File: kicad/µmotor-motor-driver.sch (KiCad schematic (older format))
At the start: 12 parts, among them Q301 FDMD82xx, Q302 FDMD82xx, Q303 FDMD82xx, U301 DRV8323S

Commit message: layout: improvements and silkscreen
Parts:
- R301, R302, R303: footprint Resistors_SMD:R_0603 -> Resistors_SMD:R_0805
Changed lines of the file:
@@
 $EndDescr
 $Comp
-L +24V #PWR015
+L +24V #PWR017
 U 1 1 59BA7201
 P 2100 2800
-F 0 "#PWR015" H 2100 2650 50  0001 C CNN
+F 0 "#PWR017" H 2100 2650 50  0001 C CNN
 F 1 "+24V" H 2100 2940 50  0000 C CNN
 F 2 "" H 2100 2800 50  0001 C CNN
@@
 $EndComp
 $Comp
-L GND #PWR016
+L GND #PWR018
 U 1 1 5A4FE4D1
 P 2300 3400
-F 0 "#PWR016" H 2300 3150 50  0001 C CNN
+F 0 "#PWR018" H 2300 3150 50  0001 C CNN
 F 1 "GND" H 2300 3250 50  0000 C CNN
 F 2 "" H 2300 3400 50  0001 C CNN
@@
 $EndComp
 $Comp
-L GND #PWR017
+L GND #PWR019
 U 1 1 5A4FE4F8
 P 2950 3400
-F 0 "#PWR017" H 2950 3150 50  0001 C CNN
+F 0 "#PWR019" H 2950 3150 50  0001 C CNN
 F 1 "GND" H 2950 3250 50  0000 C CNN
 F 2 "" H 2950 3400 50  0001 C CNN
@@
 $EndComp
 $Comp
-L GND #PWR018
+L GND #PWR020
 U 1 1 5A4FE87C
 P 4100 4000
-F 0 "#PWR018" H 4100 3750 50  0001 C CNN
+F 0 "#PWR020" H 4100 3750 50  0001 C CNN
 F 1 "GND" H 4100 3850 50  0000 C CNN
 F 2 "" H 4100 4000 50  0001 C CNN
@@
 STM32 internal pull-up!
 $Comp
-L GND #PWR019
+L GND #PWR021
 U 1 1 5A4FF46D
 P 5850 5900
-F 0 "#PWR019" H 5850 5650 50  0001 C CNN
+F 0 "#PWR021" H 5850 5650 50  0001 C CNN
 F 1 "GND" H 5850 5750 50  0000 C CNN
 F 2 "" H 5850 5900 50  0001 C CNN
@@
 $EndComp
 $Comp
-L +24V #PWR020
+L +24V #PWR022
 U 1 1 5A502CAF
 P 10100 1650
-F 0 "#PWR020" H 10100 1500 50  0001 C CNN
+F 0 "#PWR022" H 10100 1500 50  0001 C CNN
 F 1 "+24V" H 10100 1790 50  0000 C CNN
 F 2 "" H 10100 1650 50  0001 C CNN
@@
 $EndComp
 $Comp
-L +24V #PWR021
+L +24V #PWR023
 U 1 1 5A5036BC
 P 6750 2800
-F 0 "#PWR021" H 6750 2650 50  0001 C CNN
+F 0 "#PWR023" H 6750 2650 50  0001 C CNN
 F 1 "+24V" H 6750 2940 50  0000 C CNN
 F 2 "" H 6750 2800 50  0001 C CNN
@@
 $EndComp
 $Comp
-L +24V #PWR022
+L +24V #PWR024
 U 1 1 5A505C52
 P 7850 3650
-F 0 "#PWR022" H 7850 3500 50  0001 C CNN
+F 0 "#PWR024" H 7850 3500 50  0001 C CNN
 F 1 "+24V" H 7850 3790 50  0000 C CNN
 F 2 "" H 7850 3650 50  0001 C CNN
@@
 $EndComp
 $Comp
-L +24V #PWR023
+L +24V #PWR025
 U 1 1 5A50600A
 P 9000 2700
-F 0 "#PWR023" H 9000 2550 50  0001 C CNN
+F 0 "#PWR025" H 9000 2550 50  0001 C CNN
 F 1 "+24V" H 9000 2840 50  0000 C CNN
 F 2 "" H 9000 2700 50  0001 C CNN
@@
 F 0 "R302" V 9080 5600 50  0000 C CNN
 F 1 "5m" V 9000 5600 50  0000 C CNN
-F 2 "Resistors_SMD:R_0603" V 8930 5600 50  0001 C CNN
+F 2 "Resistors_SMD:R_0805" V 8930 5600 50  0001 C CNN
 F 3 "" H 9000 5600 50  0001 C CNN
 	1    9000 5600
@@
 F 0 "R303" V 10180 6000 50  0000 C CNN
 F 1 "5m" V 10100 6000 50  0000 C CNN
-F 2 "Resistors_SMD:R_0603" V 10030 6000 50  0001 C CNN
+F 2 "Resistors_SMD:R_0805" V 10030 6000 50  0001 C CNN
 F 3 "" H 10100 6000 50  0001 C CNN
 	1    10100 6000
@@
 	6750 4700 6650 4700
 $Comp
-L GND #PWR024
+L GND #PWR026
 U 1 1 5A507920
 P 10100 6350
-F 0 "#PWR024" H 10100 6100 50  0001 C CNN
+F 0 "#PWR026" H 10100 6100 50  0001 C CNN
 F 1 "GND" H 10100 6200 50  0000 C CNN
 F 2 "" H 10100 6350 50  0001 C CNN
@@
 Connection ~ 10100 5450
 $Comp
-L +3V3 #PWR025
+L +3V3 #PWR027
 U 1 1 5A521C1B
 P 4350 5100
-F 0 "#PWR025" H 4350 4950 50  0001 C CNN
+F 0 "#PWR027" H 4350 4950 50  0001 C CNN
 F 1 "+3V3" H 4350 5240 50  0000 C CNN
 F 2 "" H 4350 5100 50  0001 C CNN
@@
 F 0 "R301" V 7930 5250 50  0000 C CNN
 F 1 "5m" V 7850 5250 50  0000 C CNN
-F 2 "Resistors_SMD:R_0603" V 7780 5250 50  0001 C CNN
+F 2 "Resistors_SMD:R_0805" V 7780 5250 50  0001 C CNN
 F 3 "" H 7850 5250 50  0001 C CNN
 	1    7850 5250

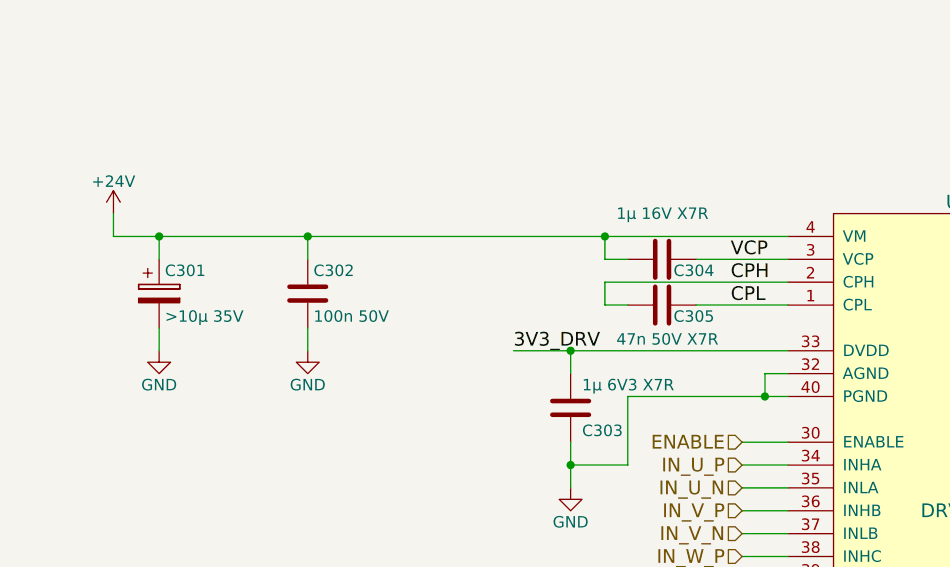
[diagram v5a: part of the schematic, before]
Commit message: add DRV8323 input cap, improve board outline
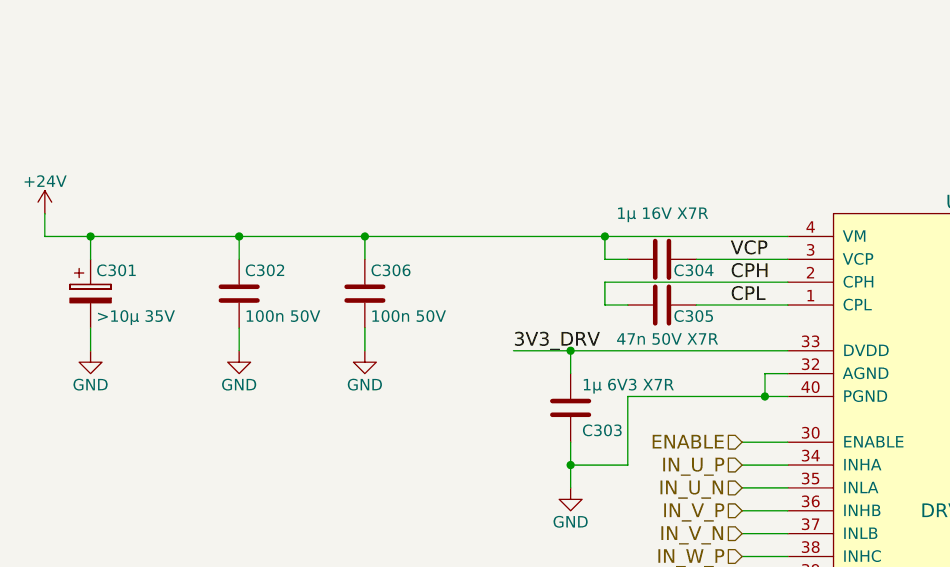
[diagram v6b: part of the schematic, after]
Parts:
- added C306: 100n 50V, Capacitors_SMD:C_0603, symbol C
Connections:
- net +24V: now also C306.1
- net GND: now also C306.2
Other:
- moved on the sheet: C301, C302
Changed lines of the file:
@@
 $EndDescr
 $Comp
-L +24V #PWR017
+L +24V #PWR301
 U 1 1 59BA7201
-P 2100 2800
-F 0 "#PWR017" H 2100 2650 50  0001 C CNN
-F 1 "+24V" H 2100 2940 50  0000 C CNN
-F 2 "" H 2100 2800 50  0001 C CNN
-F 3 "" H 2100 2800 50  0001 C CNN
-	1    2100 2800
+P 1800 2800
+F 0 "#PWR301" H 1800 2650 50  0001 C CNN
+F 1 "+24V" H 1800 2940 50  0000 C CNN
+F 2 "" H 1800 2800 50  0001 C CNN
+F 3 "" H 1800 2800 50  0001 C CNN
+	1    1800 2800
 	1    0    0    -1
 $EndComp
@@
 L C C302
 U 1 1 5A4FE3E8
-P 2950 3150
-F 0 "C302" H 2975 3250 50  0000 L CNN
-F 1 "100n 50V" H 2975 3050 50  0000 L CNN
-F 2 "Capacitors_SMD:C_0603" H 2988 3000 50  0001 C CNN
-F 3 "" H 2950 3150 50  0001 C CNN
-	1    2950 3150
+P 2650 3150
+F 0 "C302" H 2675 3250 50  0000 L CNN
+F 1 "100n 50V" H 2675 3050 50  0000 L CNN
+F 2 "Capacitors_SMD:C_0603" H 2688 3000 50  0001 C CNN
+F 3 "" H 2650 3150 50  0001 C CNN
+	1    2650 3150
 	1    0    0    -1
 $EndComp
@@
 L CP C301
 U 1 1 5A4FE464
-P 2300 3150
-F 0 "C301" H 2325 3250 50  0000 L CNN
-F 1 ">10µ 35V" H 2325 3050 50  0000 L CNN
-F 2 "Capacitors_THT:CP_Radial_D4.0mm_P2.00mm" H 2338 3000 50  0001 C CNN
-F 3 "" H 2300 3150 50  0001 C CNN
-	1    2300 3150
-	1    0    0    -1
-$EndComp
-$Comp
-L GND #PWR018
+P 2000 3150
+F 0 "C301" H 2025 3250 50  0000 L CNN
+F 1 ">10µ 35V" H 2025 3050 50  0000 L CNN
+F 2 "Capacitors_THT:CP_Radial_D4.0mm_P2.00mm" H 2038 3000 50  0001 C CNN
+F 3 "" H 2000 3150 50  0001 C CNN
+	1    2000 3150
+	1    0    0    -1
+$EndComp
+$Comp
+L GND #PWR302
 U 1 1 5A4FE4D1
-P 2300 3400
-F 0 "#PWR018" H 2300 3150 50  0001 C CNN
-F 1 "GND" H 2300 3250 50  0000 C CNN
-F 2 "" H 2300 3400 50  0001 C CNN
-F 3 "" H 2300 3400 50  0001 C CNN
-	1    2300 3400
-	1    0    0    -1
-$EndComp
-$Comp
-L GND #PWR019
+P 2000 3400
+F 0 "#PWR302" H 2000 3150 50  0001 C CNN
+F 1 "GND" H 2000 3250 50  0000 C CNN
+F 2 "" H 2000 3400 50  0001 C CNN
+F 3 "" H 2000 3400 50  0001 C CNN
+	1    2000 3400
+	1    0    0    -1
+$EndComp
+$Comp
+L GND #PWR303
 U 1 1 5A4FE4F8
-P 2950 3400
-F 0 "#PWR019" H 2950 3150 50  0001 C CNN
-F 1 "GND" H 2950 3250 50  0000 C CNN
-F 2 "" H 2950 3400 50  0001 C CNN
-F 3 "" H 2950 3400 50  0001 C CNN
-	1    2950 3400
+P 2650 3400
+F 0 "#PWR303" H 2650 3150 50  0001 C CNN
+F 1 "GND" H 2650 3250 50  0000 C CNN
+F 2 "" H 2650 3400 50  0001 C CNN
+F 3 "" H 2650 3400 50  0001 C CNN
+	1    2650 3400
 	1    0    0    -1
 $EndComp
@@
 $EndComp
 $Comp
-L GND #PWR020
+L GND #PWR305
 U 1 1 5A4FE87C
 P 4100 4000
-F 0 "#PWR020" H 4100 3750 50  0001 C CNN
+F 0 "#PWR305" H 4100 3750 50  0001 C CNN
 F 1 "GND" H 4100 3850 50  0000 C CNN
 F 2 "" H 4100 4000 50  0001 C CNN
@@
 STM32 internal pull-up!
 $Comp
-L GND #PWR021
+L GND #PWR307
 U 1 1 5A4FF46D
 P 5850 5900
-F 0 "#PWR021" H 5850 5650 50  0001 C CNN
+F 0 "#PWR307" H 5850 5650 50  0001 C CNN
 F 1 "GND" H 5850 5750 50  0000 C CNN
 F 2 "" H 5850 5900 50  0001 C CNN
@@
 $EndComp
 $Comp
-L +24V #PWR022
+L +24V #PWR311
 U 1 1 5A502CAF
 P 10100 1650
-F 0 "#PWR022" H 10100 1500 50  0001 C CNN
+F 0 "#PWR311" H 10100 1500 50  0001 C CNN
 F 1 "+24V" H 10100 1790 50  0000 C CNN
 F 2 "" H 10100 1650 50  0001 C CNN
@@
 $EndComp
 $Comp
-L +24V #PWR023
+L +24V #PWR308
 U 1 1 5A5036BC
 P 6750 2800
-F 0 "#PWR023" H 6750 2650 50  0001 C CNN
+F 0 "#PWR308" H 6750 2650 50  0001 C CNN
 F 1 "+24V" H 6750 2940 50  0000 C CNN
 F 2 "" H 6750 2800 50  0001 C CNN
@@
 $EndComp
 $Comp
-L +24V #PWR024
+L +24V #PWR309
 U 1 1 5A505C52
 P 7850 3650
-F 0 "#PWR024" H 7850 3500 50  0001 C CNN
+F 0 "#PWR309" H 7850 3500 50  0001 C CNN
 F 1 "+24V" H 7850 3790 50  0000 C CNN
 F 2 "" H 7850 3650 50  0001 C CNN
@@
 $EndComp
 $Comp
-L +24V #PWR025
+L +24V #PWR310
 U 1 1 5A50600A
 P 9000 2700
-F 0 "#PWR025" H 9000 2550 50  0001 C CNN
+F 0 "#PWR310" H 9000 2550 50  0001 C CNN
 F 1 "+24V" H 9000 2840 50  0000 C CNN
 F 2 "" H 9000 2700 50  0001 C CNN
@@
 $EndComp
 Wire Wire Line
-	2100 2900 5050 2900
-Wire Wire Line
-	2100 2900 2100 2800
+	1800 2900 5050 2900
+Wire Wire Line
+	1800 2900 1800 2800
 Wire Wire Line
 	4650 3000 5050 3000
@@
 	4250 3100 5050 3100
 Wire Wire Line
-	2950 3000 2950 2900
-Connection ~ 2950 2900
-Wire Wire Line
-	2300 3000 2300 2900
-Connection ~ 2300 2900
-Wire Wire Line
-	2950 3400 2950 3300
-Wire Wire Line
-	2300 3400 2300 3300
+	2650 3000 2650 2900
+Connection ~ 2650 2900
+Wire Wire Line
+	2000 3000 2000 2900
+Connection ~ 2000 2900
+Wire Wire Line
+	2650 3400 2650 3300
+Wire Wire Line
+	2000 3400 2000 3300
 Wire Wire Line
 	4850 3800 5050 3800
@@
 	6750 4700 6650 4700
 $Comp
-L GND #PWR026
+L GND #PWR312
 U 1 1 5A507920
 P 10100 6350
-F 0 "#PWR026" H 10100 6100 50  0001 C CNN
+F 0 "#PWR312" H 10100 6100 50  0001 C CNN
 F 1 "GND" H 10100 6200 50  0000 C CNN
 F 2 "" H 10100 6350 50  0001 C CNN
@@
 Connection ~ 10100 5450
 $Comp
-L +3V3 #PWR027
+L +3V3 #PWR306
 U 1 1 5A521C1B
 P 4350 5100
-F 0 "#PWR027" H 4350 4950 50  0001 C CNN
+F 0 "#PWR306" H 4350 4950 50  0001 C CNN
 F 1 "+3V3" H 4350 5240 50  0000 C CNN
 F 2 "" H 4350 5100 50  0001 C CNN
@@
 3V3_DRV
 Connection ~ 4100 3400
+$Comp
+L C C306
+U 1 1 5A78F36A
+P 3200 3150
+F 0 "C306" H 3225 3250 50  0000 L CNN
+F 1 "100n 50V" H 3225 3050 50  0000 L CNN
+F 2 "Capacitors_SMD:C_0603" H 3238 3000 50  0001 C CNN
+F 3 "" H 3200 3150 50  0001 C CNN
+	1    3200 3150
+	1    0    0    -1
+$EndComp
+$Comp
+L GND #PWR304
+U 1 1 5A78F370
+P 3200 3400
+F 0 "#PWR304" H 3200 3150 50  0001 C CNN
+F 1 "GND" H 3200 3250 50  0000 C CNN
+F 2 "" H 3200 3400 50  0001 C CNN
+F 3 "" H 3200 3400 50  0001 C CNN
+	1    3200 3400
+	1    0    0    -1
+$EndComp
+Wire Wire Line
+	3200 3400 3200 3300
+Wire Wire Line
+	3200 3000 3200 2900
+Connection ~ 3200 2900
 $EndSCHEMATC
